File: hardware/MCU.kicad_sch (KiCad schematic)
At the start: 28 parts, among them Q1 2N2219, Q2 2N2219, SW2 GPIO_N_RST, SW3 SW_SYS-PWR, SW4 GPIO_HW_ADDR_SEL, U3 SX1509BIULTRT

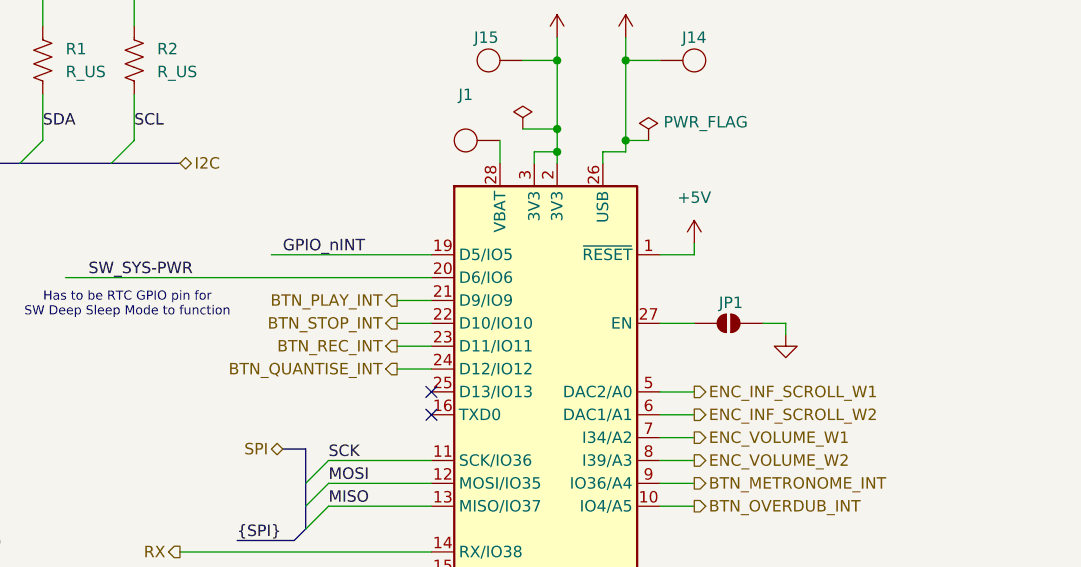
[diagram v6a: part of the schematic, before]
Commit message: fix [HWE]: Update SPI OLED RES and DC connections
The RES pin of the OLED display is now connected to the RESET pin of the MCU, the DC pin will be routed to the GPIO pin D13 (at the cost of continually driving the BUILITIN LED)
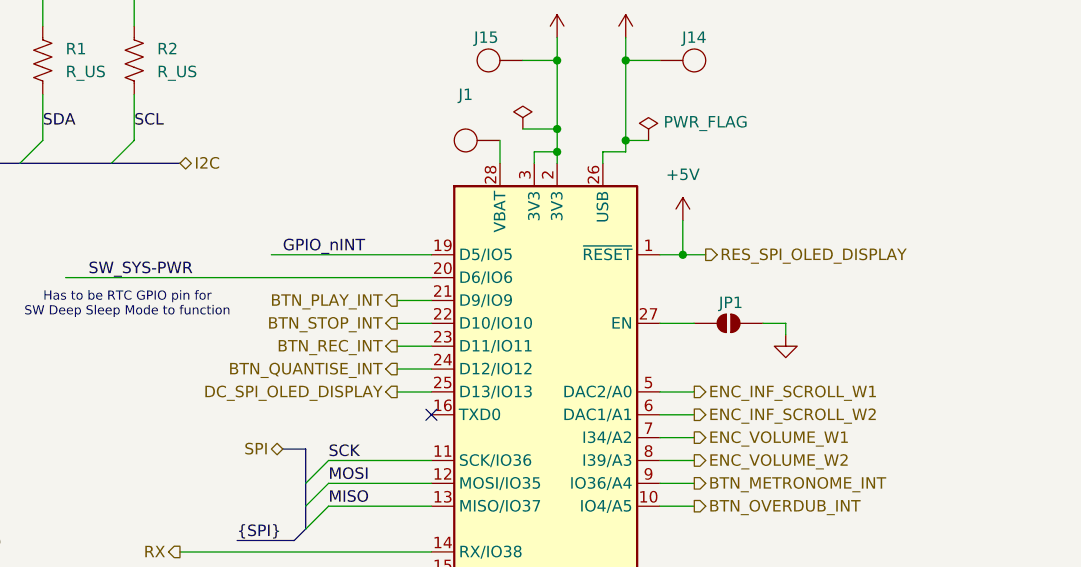
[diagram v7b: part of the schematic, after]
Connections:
- net DC_SPI_OLED_DISPLAY: now reaches A2.25 (D13/IO13)
- no-connect marks 12 -> 11
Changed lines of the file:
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@@
+	)
+	(junction
+		(at 220.98 53.34)
+		(diameter 0)
+		(color 0 0 0 0)
 	)
 	(junction
@@
 	)
 	(no_connect
-		(at 193.04 68.58)
-	)
-	(no_connect
 		(at 78.74 68.58)
 	)
@@
 		)
 	)
+	(wire
+		(pts
+			(xy 189.23 68.58) (xy 193.04 68.58)
+		)
+		(stroke
+			(width 0)
+			(type default)
+		)
+	)
 	(bus
 		(pts
@@
 	(wire
 		(pts
+			(xy 220.98 53.34) (xy 223.52 53.34)
+		)
+		(stroke
+			(width 0)
+			(type default)
+		)
+	)
+	(wire
+		(pts
 			(xy 60.96 171.45) (xy 83.82 171.45)
 		)
@@
 	(wire
 		(pts
-			(xy 222.25 52.07) (xy 222.25 53.34)
+			(xy 220.98 49.53) (xy 220.98 53.34)
 		)
 		(stroke
@@
 	(wire
 		(pts
-			(xy 218.44 53.34) (xy 222.25 53.34)
+			(xy 218.44 53.34) (xy 220.98 53.34)
 		)
 		(stroke
@@
 			)
 			(justify right)
+		)
+	)
+	(hierarchical_label "DC_SPI_OLED_DISPLAY"
+		(shape output)
+		(at 189.23 68.58 180)
+		(effects
+			(font
+				(size 1.27 1.27)
+			)
+			(justify right)
+		)
+	)
+	(hierarchical_label "RES_SPI_OLED_DISPLAY"
+		(shape output)
+		(at 223.52 53.34 0)
+		(effects
+			(font
+				(size 1.27 1.27)
+			)
+			(justify left)
 		)
 	)
@@
 	(symbol
 		(lib_id "4ms_Power-symbol:+5V")
-		(at 222.25 52.07 0)
+		(at 220.98 49.53 0)
 		(unit 1)
 		(exclude_from_sim no)
@@
 		(fields_autoplaced yes)
 		(property "Reference" "#PWR04"
-			(at 222.25 55.88 0)
+			(at 220.98 53.34 0)
 			(effects
 				(font
@@
 		)
 		(property "Value" "+5V"
-			(at 222.25 46.99 0)
+			(at 220.98 44.45 0)
 			(effects
 				(font
@@
 		)
 		(property "Footprint" ""
-			(at 222.25 52.07 0)
+			(at 220.98 49.53 0)
 			(effects
 				(font
@@
 		)
 		(property "Datasheet" ""
-			(at 222.25 52.07 0)
+			(at 220.98 49.53 0)
 			(effects
 				(font
@@
 		)
 		(property "Description" ""
-			(at 222.25 52.07 0)
-			(effects
-				(font
+			(at 220.98 49.53 0)
+			(effects
+				(font

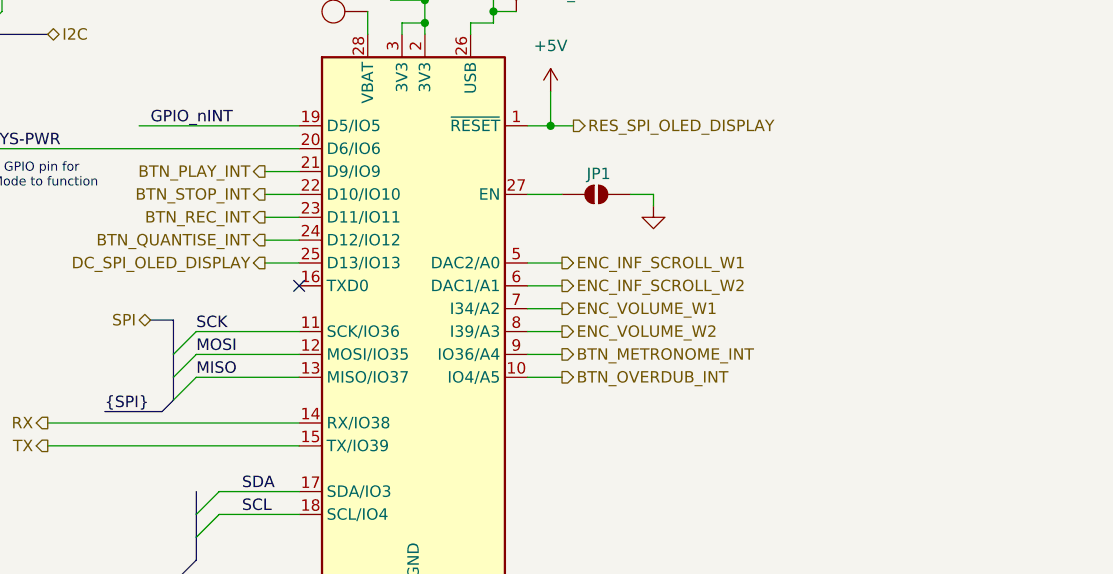
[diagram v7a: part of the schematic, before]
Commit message: feat [HWE]: Added probe points to SPI connections
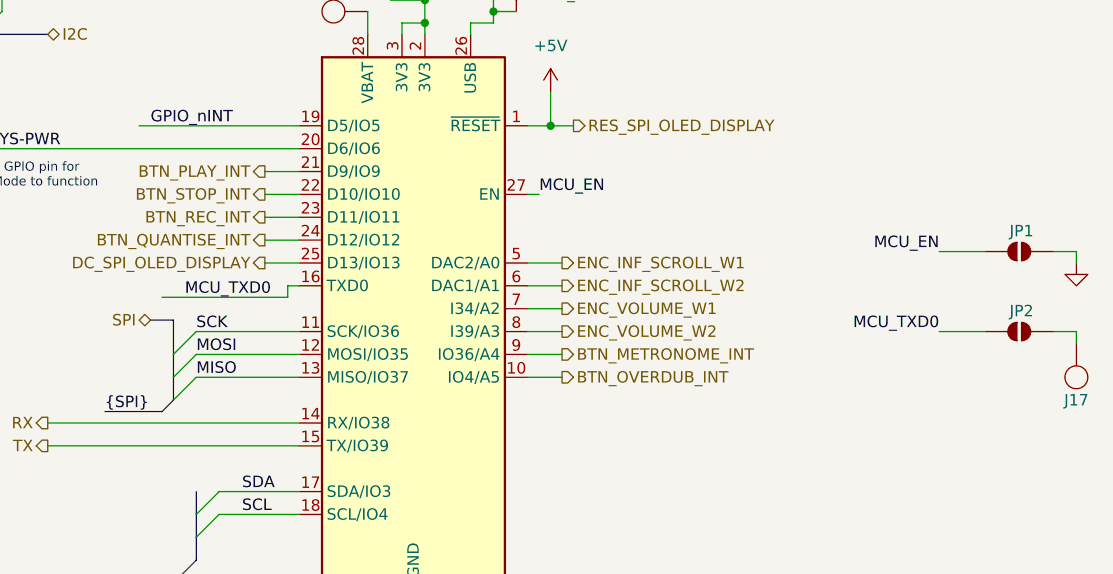
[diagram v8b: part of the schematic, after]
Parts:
- added J17: ~, 4ms_Connector:CAPSENSE_PAD, symbol 4ms_Connector:CAPSENSE_PAD
- added JP2: SolderJumper_2_Open, Jumper:SolderJumper-2_P1.3mm_Open_Pad1.0x1.5mm, symbol Jumper:SolderJumper_2_Open
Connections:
- net MCU_EN: now reaches A2.27 (EN), JP1.1 (A)
- net MCU_TXD0: now reaches A2.16 (TXD0)
- net MCU_TXD0: now also JP2.1 (A)
- new net: J17.1 (CS), JP2.2 (B)
- no-connect marks 11 -> 10
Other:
- moved on the sheet: JP1
